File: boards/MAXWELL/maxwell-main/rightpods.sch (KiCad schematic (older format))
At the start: 14 parts

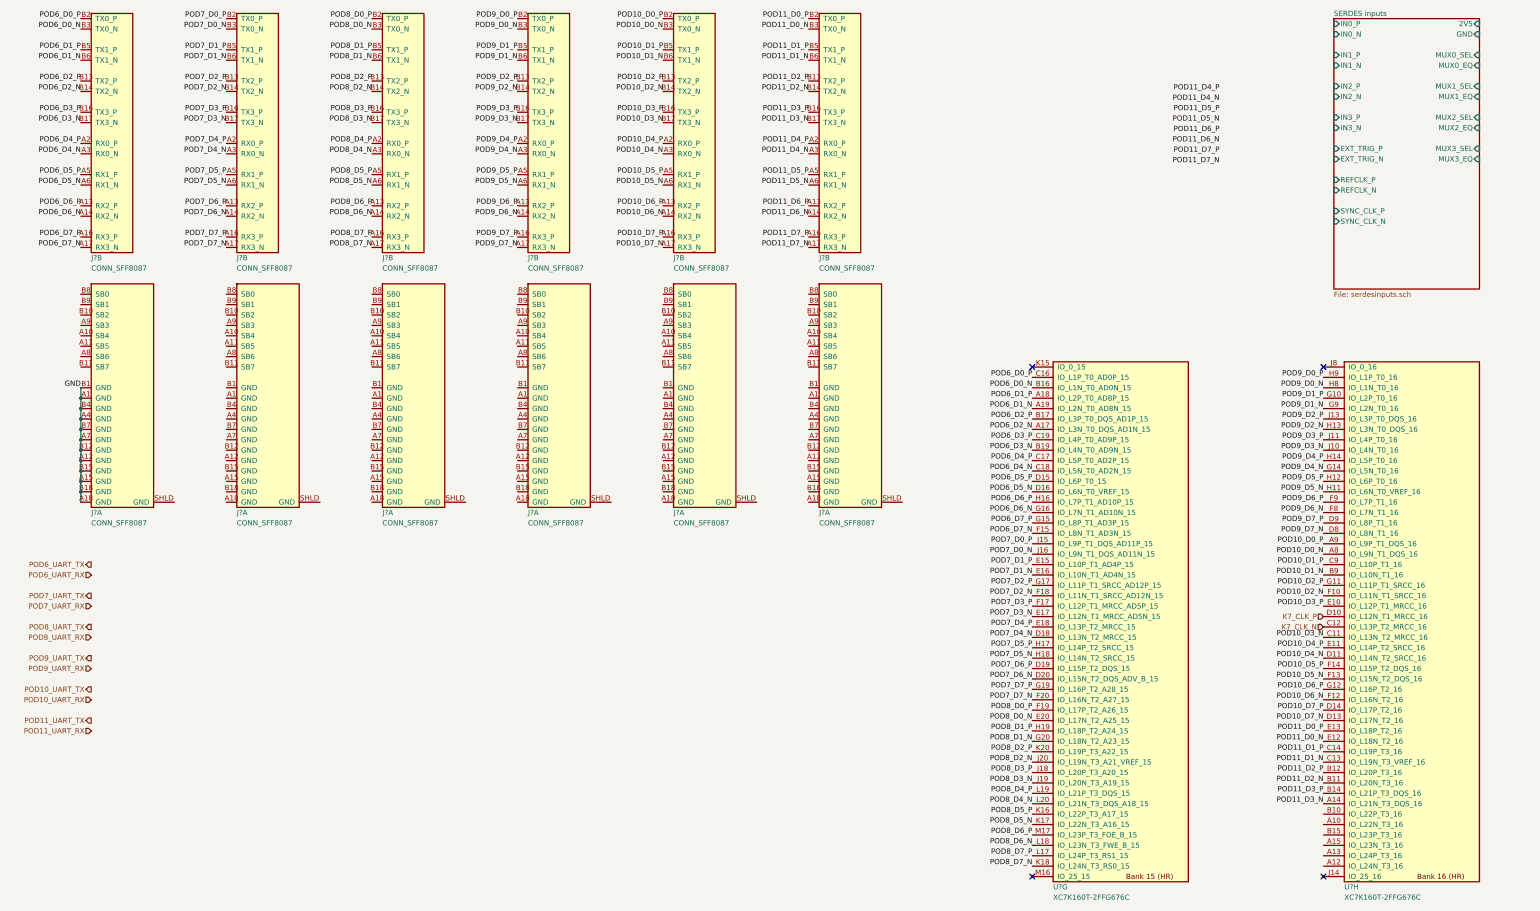
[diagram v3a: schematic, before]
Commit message: Continued initial schematic capture
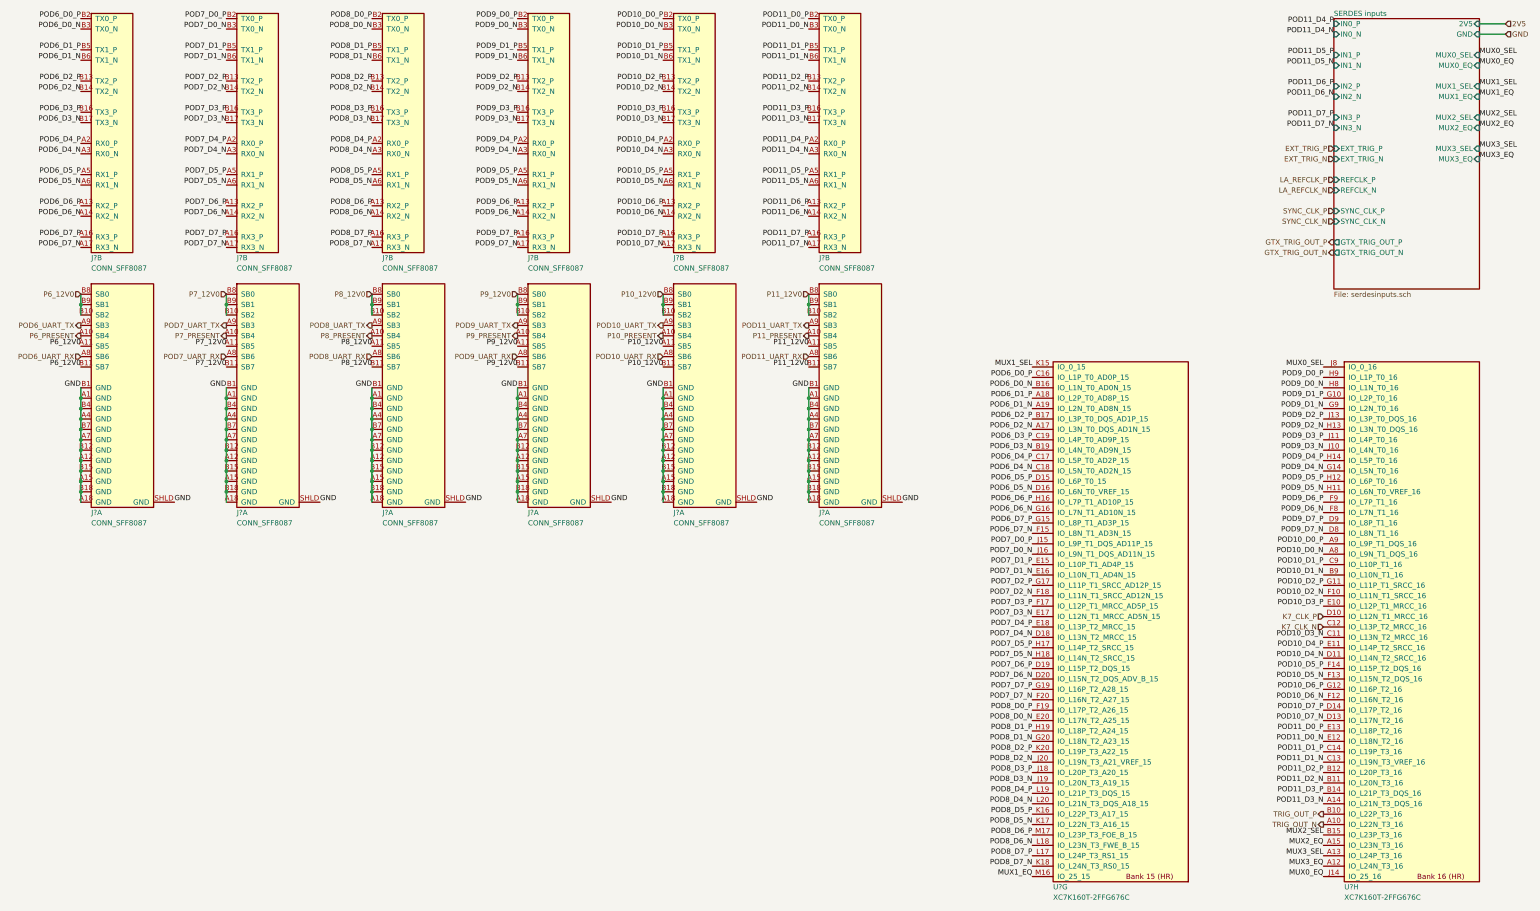
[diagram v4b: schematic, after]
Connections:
- net GND: now also J?.A1 (GND), J?.A1 (GND), J?.A1 (GND), J?.A1 (GND), J?.A1 (GND), J?.A12 (GND), J?.A12 (GND), J?.A12 (GND), J?.A12 (GND), J?.A12 (GND), J?.A15 (GND), J?.A15 (GND), J?.A15 (GND), J?.A15 (GND), J?.A15 (GND), J?.A18 (GND), J?.A18 (GND), J?.A18 (GND), J?.A18 (GND), J?.A18 (GND), J?.A4 (GND), J?.A4 (GND), J?.A4 (GND), J?.A4 (GND), J?.A4 (GND), J?.A7 (GND), J?.A7 (GND), J?.A7 (GND), J?.A7 (GND), J?.A7 (GND), J?.B1 (GND), J?.B1 (GND), J?.B1 (GND), J?.B1 (GND), J?.B1 (GND), J?.B12 (GND), J?.B12 (GND), J?.B12 (GND), J?.B12 (GND), J?.B12 (GND), J?.B15 (GND), J?.B15 (GND), J?.B15 (GND), J?.B15 (GND), J?.B15 (GND), J?.B18 (GND), J?.B18 (GND), J?.B18 (GND), J?.B18 (GND), J?.B18 (GND), J?.B4 (GND), J?.B4 (GND), J?.B4 (GND), J?.B4 (GND), J?.B4 (GND), J?.B7 (GND), J?.B7 (GND), J?.B7 (GND), J?.B7 (GND), J?.B7 (GND), J?.SHLD (GND), J?.SHLD (GND), J?.SHLD (GND), J?.SHLD (GND), J?.SHLD (GND), J?.SHLD (GND)
- net POD10_UART_RX: now also J?.A8 (SB6)
- net POD10_UART_TX: now also J?.A9 (SB3)
- net POD11_UART_RX: now also J?.A8 (SB6)
- net POD11_UART_TX: now also J?.A9 (SB3)
- net POD6_UART_RX: now also J?.A8 (SB6)
- net POD6_UART_TX: now also J?.A9 (SB3)
- net POD7_UART_RX: now also J?.A8 (SB6)
- net POD7_UART_TX: now also J?.A9 (SB3)
- net POD8_UART_RX: now also J?.A8 (SB6)
- net POD8_UART_TX: now also J?.A9 (SB3)
- net POD9_UART_RX: now also J?.A8 (SB6)
- net POD9_UART_TX: now also J?.A9 (SB3)
- net MUX1_SEL: now reaches U?.K15 (IO_0_15)
- net MUX1_EQ: now reaches U?.M16 (IO_25_15)
- net TRIG_OUT_N: now reaches U?.A10 (IO_L22N_T3_16)
- net MUX3_EQ: now reaches U?.A12 (IO_L24N_T3_16)
- net MUX3_SEL: now reaches U?.A13 (IO_L24P_T3_16)
- net MUX2_EQ: now reaches U?.A15 (IO_L23N_T3_16)
- net TRIG_OUT_P: now reaches U?.B10 (IO_L22P_T3_16)
- net MUX2_SEL: now reaches U?.B15 (IO_L23P_T3_16)
- net MUX0_EQ: now reaches U?.J14 (IO_25_16)
- net MUX0_SEL: now reaches U?.J8 (IO_0_16)
- net P6_PRESENT: now reaches J?.A10 (SB4)
- net P6_12V0: now reaches J?.A11 (SB5)
- net P6_12V0: now also J?.B10 (SB2), J?.B11 (SB7), J?.B8 (SB0), J?.B9 (SB1)
- net P7_PRESENT: now reaches J?.A10 (SB4)
- net P7_12V0: now reaches J?.A11 (SB5)
- net P7_12V0: now also J?.B10 (SB2), J?.B11 (SB7), J?.B8 (SB0), J?.B9 (SB1)
- net P8_PRESENT: now reaches J?.A10 (SB4)
- net P8_12V0: now reaches J?.A11 (SB5)
- net P8_12V0: now also J?.B10 (SB2), J?.B11 (SB7), J?.B8 (SB0), J?.B9 (SB1)
- net P9_PRESENT: now reaches J?.A10 (SB4)
- net P9_12V0: now reaches J?.A11 (SB5)
- net P9_12V0: now also J?.B10 (SB2), J?.B11 (SB7), J?.B8 (SB0), J?.B9 (SB1)
- net P10_PRESENT: now reaches J?.A10 (SB4)
- net P10_12V0: now reaches J?.A11 (SB5)
- net P10_12V0: now also J?.B10 (SB2), J?.B11 (SB7), J?.B8 (SB0), J?.B9 (SB1)
- net P11_PRESENT: now reaches J?.A10 (SB4)
- net P11_12V0: now reaches J?.A11 (SB5)
- net P11_12V0: now also J?.B10 (SB2), J?.B11 (SB7), J?.B8 (SB0), J?.B9 (SB1)
- no-connect marks 4 -> 0
